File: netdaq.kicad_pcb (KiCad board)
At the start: 4 copper layers, 80 x 89 mm, 516 parts, among them CN1 HX JN1.27-2X5P ZZ H4.9, J1 RJ45, J3 Conn_01x06_Pin, J4 Micro_SD_Card_Det2, Q3 BSS138LT1G, Q4 BSS138LT1G, Q5 BSS138LT1G, Q6 BSS138LT1G, SW1 TS110926043, SW2 TS110926043, T2 POE30P-50L, U1 PIC32CK1025GC01100-I/4SB, U10 TLA2518IRTER, U11 TLA2518IRTER, U12 PD70100ILD-TR, U13 DLM0NSN500HY2D, U2 LAN8720A-CP, U5 MP6004GQ-P, U6 TPUSBLC6-4SC6, U7 TPS62A01PDDCR, U8 TLA2518IRTER, U9 TLA2518IRTER, Y4 Crystal_GND24

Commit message: many stuffs
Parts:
- removed J1: RJ45, Connector_RJ:RJ45_Amphenol_54602-x08_Horizontal
- removed J4: Micro_SD_Card_Det2, Connector_Card:microSD_HC_Hirose_DM3AT-SF-PEJM5
- removed TR1: PT61017PEL, Transformer_SMD:Transformer_Ethernet_Bourns_PT61017PEL
- added C129: 100n, Capacitor_SMD:C_0402_1005Metric, F.Cu at (202.0, 127.0)
- added C130: 100n, Capacitor_SMD:C_0402_1005Metric, F.Cu at (200.5, 122.5)
- added RJ1: HC-WK88-H16-DB, C7501824:RJ45-TH_HC-WK88-H16-DB, F.Cu at (145.5, 64.0)
- added T1: H1102NLT, C18584:XFMR-SMD_H1102NLT, F.Cu at (145.0, 76.5)
- added TP180: TestPoint, TestPoint:TestPoint_THTPad_D1.0mm_Drill0.5mm, F.Cu at (185.3, 57.0)
- added TP181: TestPoint, TestPoint:TestPoint_THTPad_D1.0mm_Drill0.5mm, F.Cu at (164.0, 69.0)
- added TP182: TestPoint_Alt, TestPoint:TestPoint_THTPad_1.0x1.0mm_Drill0.5mm, F.Cu at (208.8, 114.8)
- added U14: TXU0202DCUR, C5186957:VSSOP-8_L2.3-W2.0-P0.50-LS3.1-BR, F.Cu at (202.5, 123.5)
- added U15: MLD-TF PUSH-H18, C52750848:SD-SMD_MLD-TF-PUSH-H18, F.Cu at (137.4, 108.5)
- moved TP66 123.0 mm to (114.0, 93.8)
- moved TP90 118.2 mm to (140.8, 137.8)
- moved TP68 117.1 mm to (119.8, 94.2)
- moved TP60 116.5 mm to (117.5, 91.0)
- moved TP91 115.0 mm to (142.8, 137.8)
- moved TP92 111.8 mm to (144.8, 137.8)
- moved TP56 111.6 mm to (122.2, 87.5)
- moved TP58 108.8 mm to (125.0, 91.5)
- moved TP93 108.7 mm to (146.8, 137.8)
- moved TP97 108.7 mm to (154.8, 137.8)
- moved TP62 108.5 mm to (125.8, 94.0)
- moved TP45 106.0 mm to (122.5, 93.8)
- moved TP94 105.6 mm to (148.8, 137.8)
- moved TP89 105.4 mm to (135.5, 67.2)
- moved TP98 105.4 mm to (156.8, 137.8)
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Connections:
- net /Debug Connector/NC_DBG_UART_CTS# renamed /Debug Connector/NC_UART_CTS#
- net /Debug Connector/NC_DBG_UART_RTS# renamed /Debug Connector/NC_UART_RTS#
- net /Debug Connector/NC_DBG_UART_VCC renamed /Debug Connector/EXT_UART_VCC
- J3 pad 4: /Debug Connector/UART.TX -> /Debug Connector/EXT_UART_TX
- J3 pad 5: /Debug Connector/UART.RX -> /Debug Connector/EXT_UART_RX
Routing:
- net /Ethernet Connector/POE_V-: track 27.2 -> 9.14 mm
- net /USB.D+: track 62.8 -> 46.1 mm
- net /Ethernet Connector/MX2-: track 5.58 -> 21.7 mm
- net /USB.D-: track 61.7 -> 47.0 mm
- net /Ethernet Connector/MX3-: track 16.8 -> 30.5 mm
- net GND: track 39.7 -> 50.6 mm, vias 35 -> 192
- net /MCU_SPI3_ADC2.SCK: track 13.3 -> 24.0 mm, vias 0 -> 1
- net /MCU_SPI3_ADC2.CS#: track 11.8 -> 21.9 mm, vias 0 -> 1
- net /Ethernet Connector/MX4-: track 20.8 -> 30.9 mm, vias 0 -> 2
- net +3.3V: track 37.0 -> 46.3 mm, vias 45 -> 58
- net /MCU/USB_FS.D-: track 11.1 -> 19.8 mm
- net /MCU_SPI3_ADC2.MISO: track 12.1 -> 20.7 mm, vias 2 -> 1
- net /DAQ Connector/EXT_ADC1: track 5.92 -> 14.5 mm
- net /GPIO1: track 19.2 -> 27.5 mm
- net /Debug Connector/UART.RX: track 0.00 -> 8.27 mm
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- added copper zone on F.Cu, net +VADC
- added copper zone on In1.Cu, net +VADC
- added copper zone on F.Cu, net /Debug Connector/EXT_UART_VCC
- added copper zone on B.Cu, net ETH_SHIELD
- added copper zone on F.Cu, net ETH_SHIELD
- added copper zone on In1.Cu, net ETH_SHIELD
- added copper zone on In2.Cu, net ETH_SHIELD
- added copper zone on F.Cu, net Net-(U10-AVDD)
- added copper zone on F.Cu, net Net-(U10-DECAP)
- added copper zone on F.Cu, net Net-(U10-DVDD)
- added copper zone on F.Cu, net Net-(U11-AVDD)
- added copper zone on F.Cu, net Net-(U11-DECAP)
- added copper zone on F.Cu, net Net-(U11-DVDD)
- added copper zone on F.Cu, net Net-(U8-AVDD)
- added copper zone on F.Cu, net Net-(U8-DECAP)
- added copper zone on F.Cu, net Net-(U8-DVDD)
- added copper zone on F.Cu, net Net-(U9-AVDD)
- added copper zone on F.Cu, net Net-(U9-DECAP)
- added copper zone on F.Cu, net Net-(U9-DVDD)

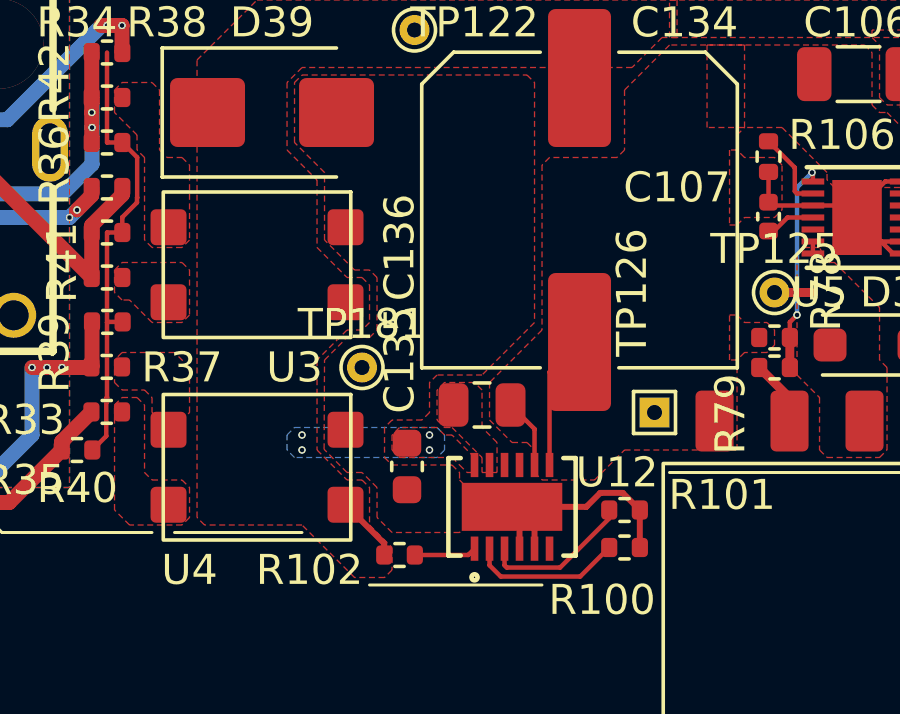
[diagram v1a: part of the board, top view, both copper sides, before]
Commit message: did a bunch of bom matching to lcsc
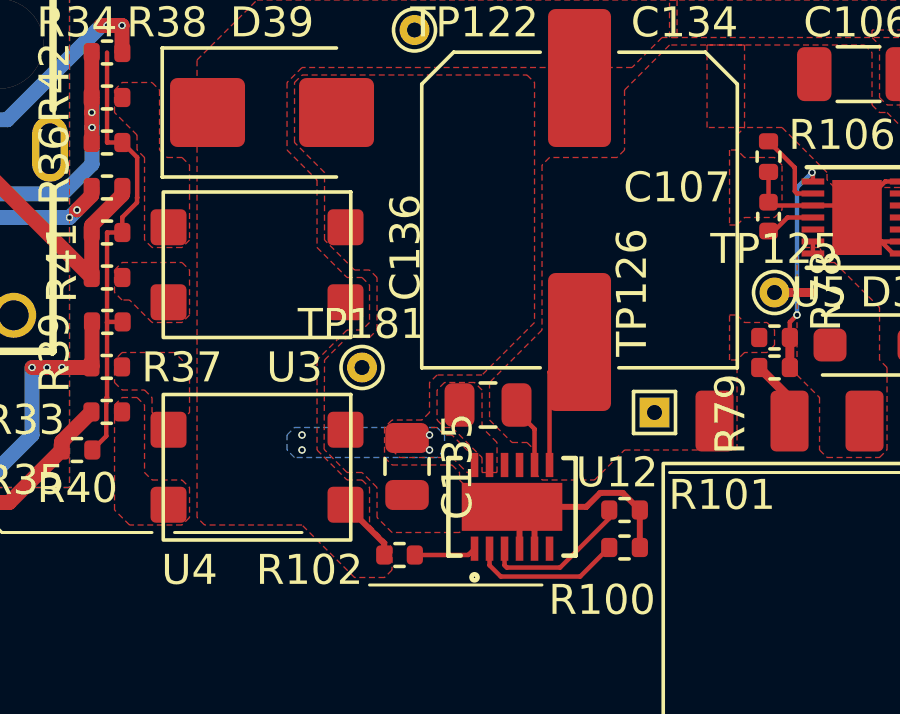
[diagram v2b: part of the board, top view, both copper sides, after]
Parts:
- C1, C136: value 4.7u -> 4.7u 25V
- C10, C11, C114, C12, C129, C13, C130, C14, C16, C17, C18, C2, C26, C28, C30, C34, C35, C5, C7, C8, C9: value 100n -> 100n 50V
- C109, C110, C111, C112, C113, C4: value 10u -> 10u 25V
- C115, C116, C117, C118, C119, C120, C121, C122, C123, C124, C125, C126, C25, C27, C29, C31: value 1u -> 1u 50V
- C127: value 100n 10V -> 100n 50V
- C135: footprint Capacitor_SMD:C_0603_1608Metric -> Capacitor_SMD:C_0805_2012Metric
- C32: value 470p -> 470p 50V
- moved C136 0.20 mm to (168.2, 70.2)

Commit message: did almost nothing!
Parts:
- added C33: 1n 2000V, Capacitor_SMD:C_1206_3216Metric, F.Cu at (163.8, 38.4)
- added C36: 1n 2000V, Capacitor_SMD:C_1206_3216Metric, F.Cu at (163.8, 41.8)
- added C37: 1n 2000V, Capacitor_SMD:C_1206_3216Metric, F.Cu at (163.8, 45.1)
- added D79: D_Schottky, Diode_SMD:D_SOD-323, F.Cu at (192.7, 84.5)
- added D81: D_Schottky, Diode_SMD:D_SOD-323, F.Cu at (223.2, 91.0)
- added R32: 1M, Resistor_SMD:R_1206_3216Metric, F.Cu at (169.4, 38.4)
- added R43: 1M, Resistor_SMD:R_1206_3216Metric, F.Cu at (169.4, 41.7)
- added TP135: TestPoint_Alt, TestPoint:TestPoint_THTPad_1.0x1.0mm_Drill0.5mm, F.Cu at (226.8, 88.1)
- C103, C104: value 22u 10 V -> 22u 25 V
- C107: value 1u 10V -> 1u 25V
- C128: value 10u 10V -> 10u 25V
- C15, C3, C6: footprint Capacitor_SMD:C_1210_3225Metric -> Capacitor_SMD:C_1206_3216Metric
- R100, R104, R3, R4, R5, R6, R8: footprint Resistor_SMD:R_0402_1005Metric -> Resistor_SMD:R_0603_1608Metric
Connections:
- C109 pad 1: +5.0V -> Net-(D79-K)
- R82 pad 2: +5.0V -> Net-(D79-K)
- TP133 pad 1: +5.0V -> Net-(D79-K)
- U7 pad 4: +5.0V -> Net-(D79-K)
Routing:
- net Net-(D79-K): track 0.00 -> 0.91 mm, vias 0 -> 1
- net +5.0V: track 8.01 -> 7.10 mm, vias 1 -> 0
